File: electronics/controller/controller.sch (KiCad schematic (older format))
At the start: 25 parts

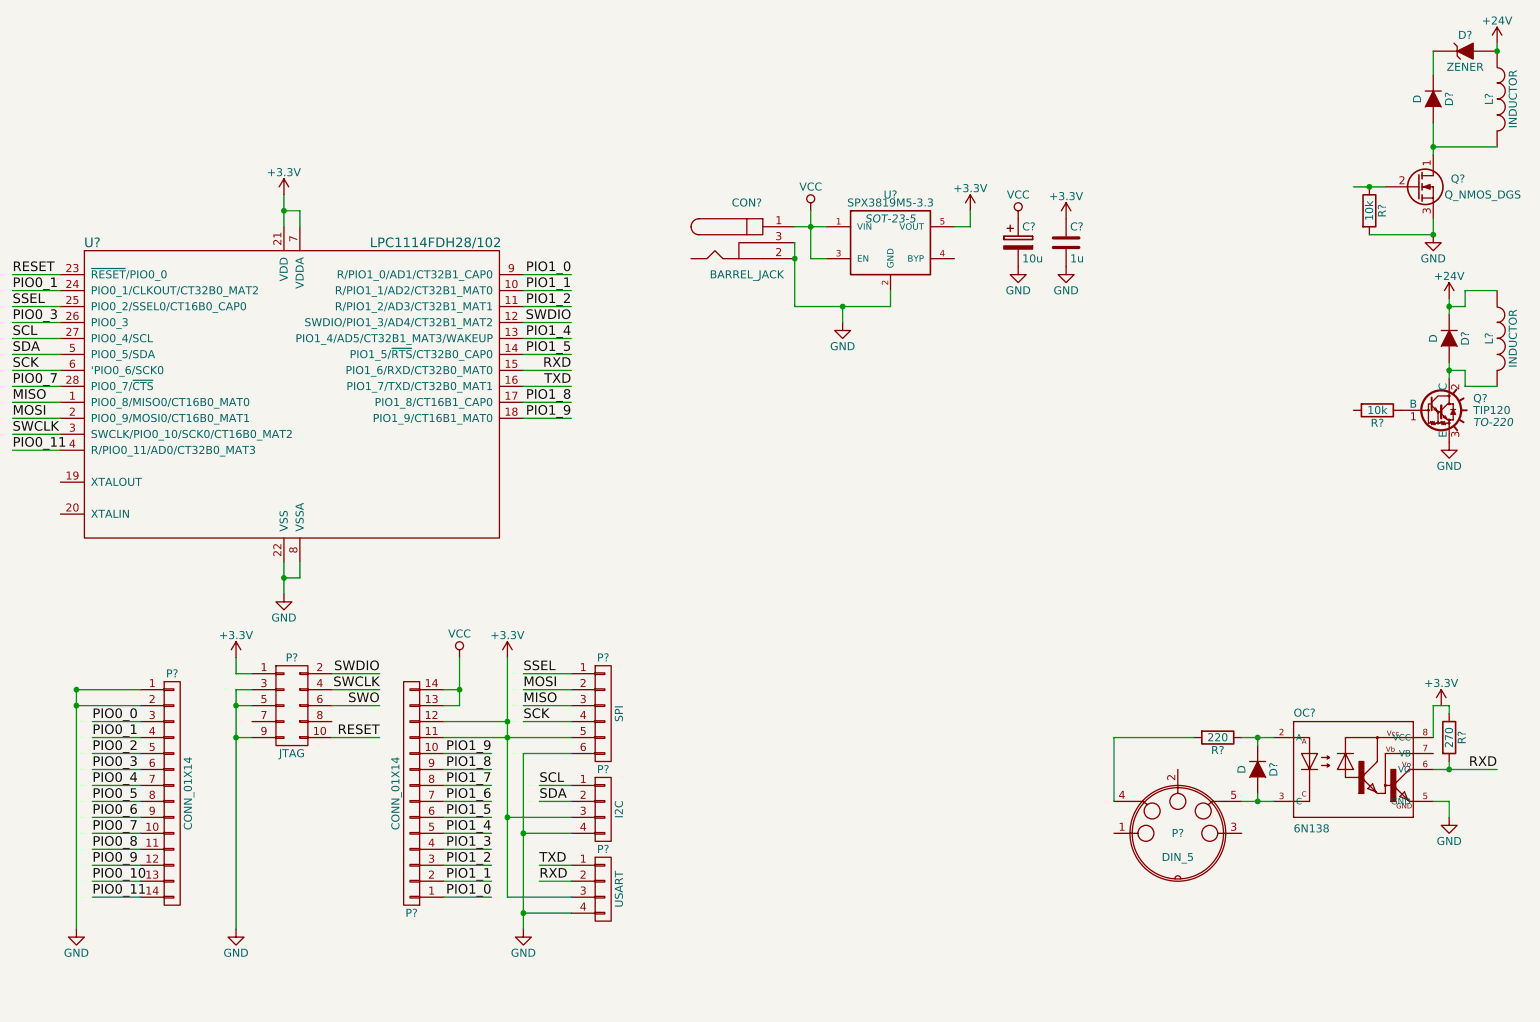
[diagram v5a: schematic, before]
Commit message: Add NFET for reverse polarity protection
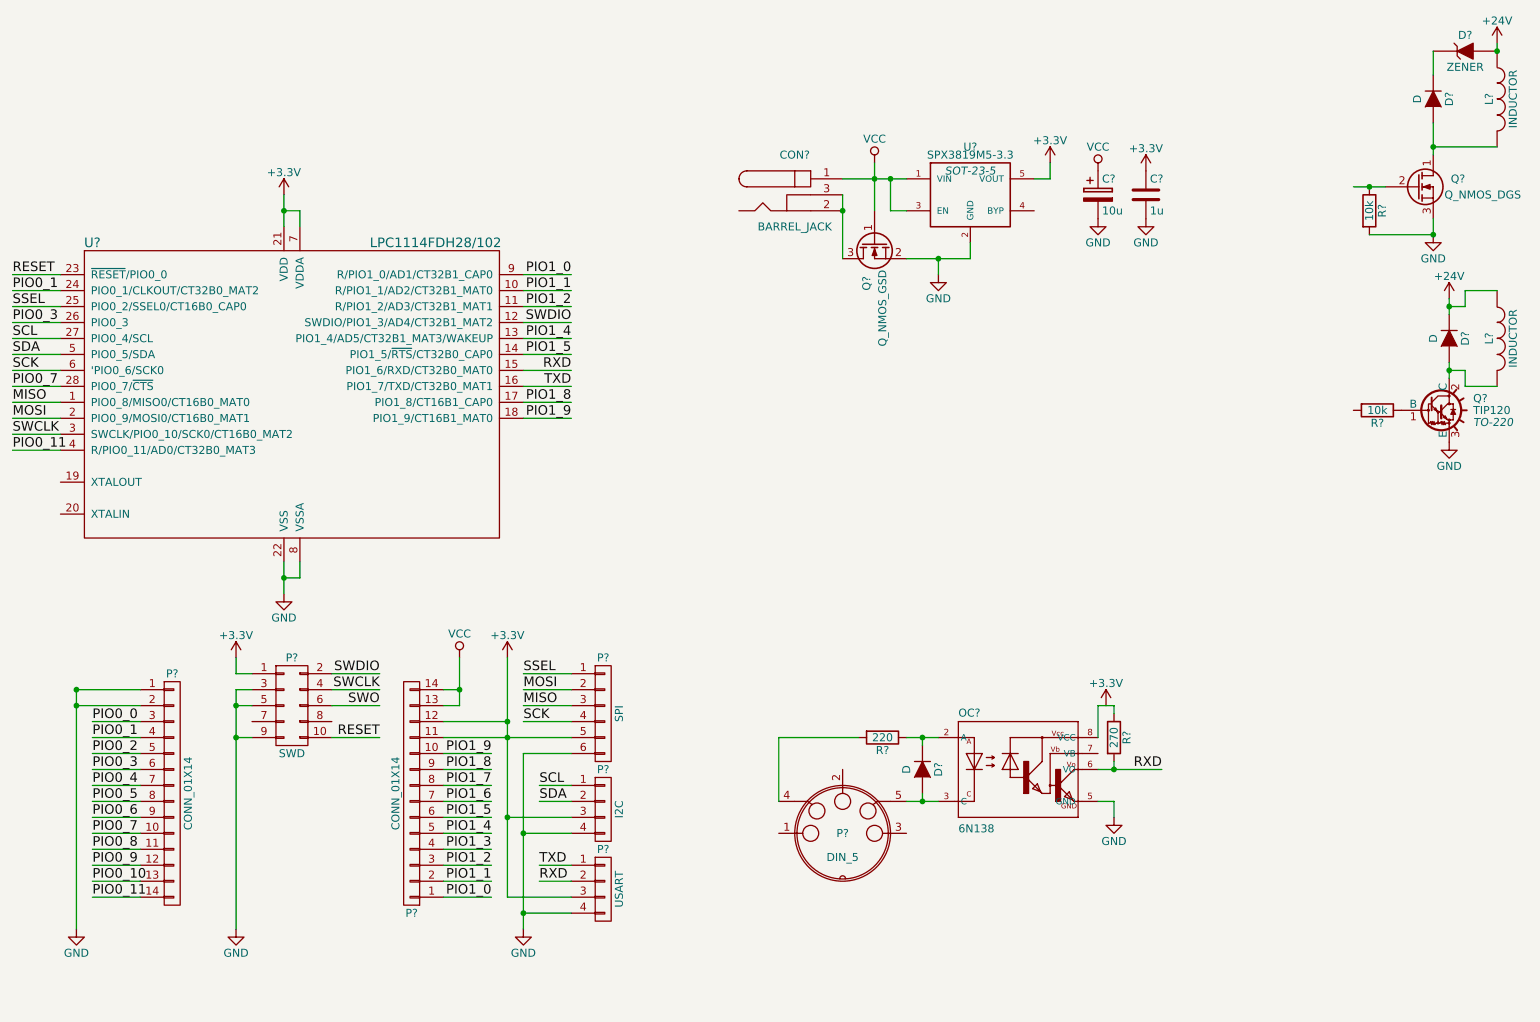
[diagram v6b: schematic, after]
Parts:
- added Q?: Q_NMOS_GSD, symbol Q_NMOS_GSD
- P?: value JTAG -> SWD
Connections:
- net GND: now also Q?.2 (S); no longer CON?.2, CON?.3
- net VCC: now also Q?.1 (G)
- new net: CON?.2, CON?.3, Q?.3 (D)
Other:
- moved on the sheet: C?, CON?, D?, OC?, P?, R?, U?

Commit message: Remove MIDI and solenoid circuits
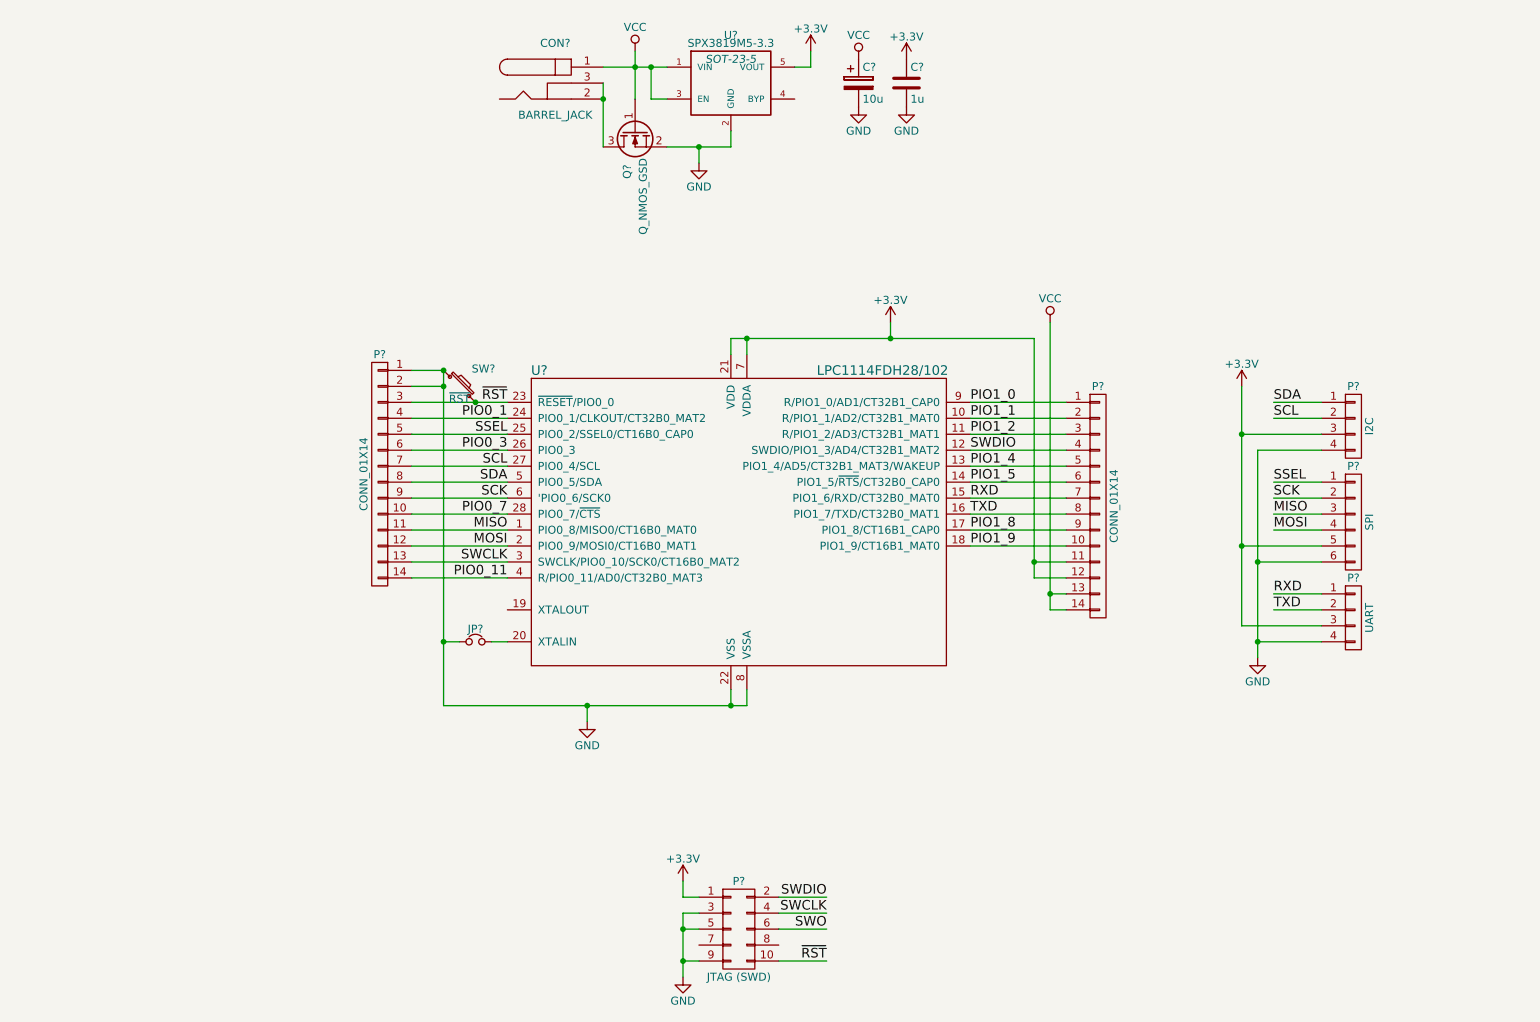
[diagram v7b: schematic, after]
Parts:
- removed D? (x3): D, symbol D
- removed D?: ZENER, symbol ZENER
- removed L? (x2): INDUCTOR, symbol INDUCTOR
- removed OC?: 6N138, optocoupler-DIL08, symbol 6N138
- removed P?: DIN_5, symbol DIN_5
- removed Q?: Q_NMOS_DGS, symbol Q_NMOS_DGS
- removed Q?: TIP120, TO-220, symbol TIP120
- removed R?: 270, symbol R
- removed R?: 220, symbol R
- removed R? (x2): 10k, symbol R
- added JP?: Jumper_NC_Small, symbol Jumper_NC_Small
- added SW?: ~RST~, symbol SW_PUSH_SMALL
- P?: value SWD -> JTAG (SWD)
- P?: value USART -> UART
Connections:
- net PIO0_10 is gone; now on net SWCLK: P?.13 (P13)
- net PIO0_2 is gone; now on net SSEL: P?.5 (P5)
- net PIO0_4 is gone; now on net SCL: P?.7 (P7)
- net PIO0_5 is gone; now on net SDA: P?.8 (P8)
- net PIO0_6 is gone; now on net SCK: P?.9 (P9)
- net PIO0_8 is gone; now on net MISO: P?.11 (P11)
- net PIO0_9 is gone; now on net MOSI: P?.12 (P12)
- net PIO1_3 is gone; now on net SWDIO: P?.4 (P4)
- net PIO1_6 is gone; now on net RXD: P?.7 (P7)
- net PIO1_7 is gone; now on net TXD: P?.8 (P8)
- net RESET is gone; now on net ~RST~: P?.10 (P10), U?.23 (~RESET~/PIO0_0)
- net GND: now also JP?.1, SW?.1
- net MOSI: now also P?.4 (P4); no longer P?.2 (P2)
- net RXD: now also P?.1 (P1); no longer P?.2 (P2)
- net SCK: now also P?.2 (P2); no longer P?.4 (P4)
- net SCL: now also P?.2 (P2); no longer P?.1 (P1)
- net SDA: now also P?.1 (P1); no longer P?.2 (P2)
- net TXD: now also P?.2 (P2); no longer P?.1 (P1)
- net at U?.20 (XTALIN): now also JP?.2
- net PIO0_0 renamed ~RST~
- net ~RST~: now also SW?.2
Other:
- moved on the sheet: C?, CON?, P?, Q?, U?

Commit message: Add LED on PIO0_7 (high-drive output)
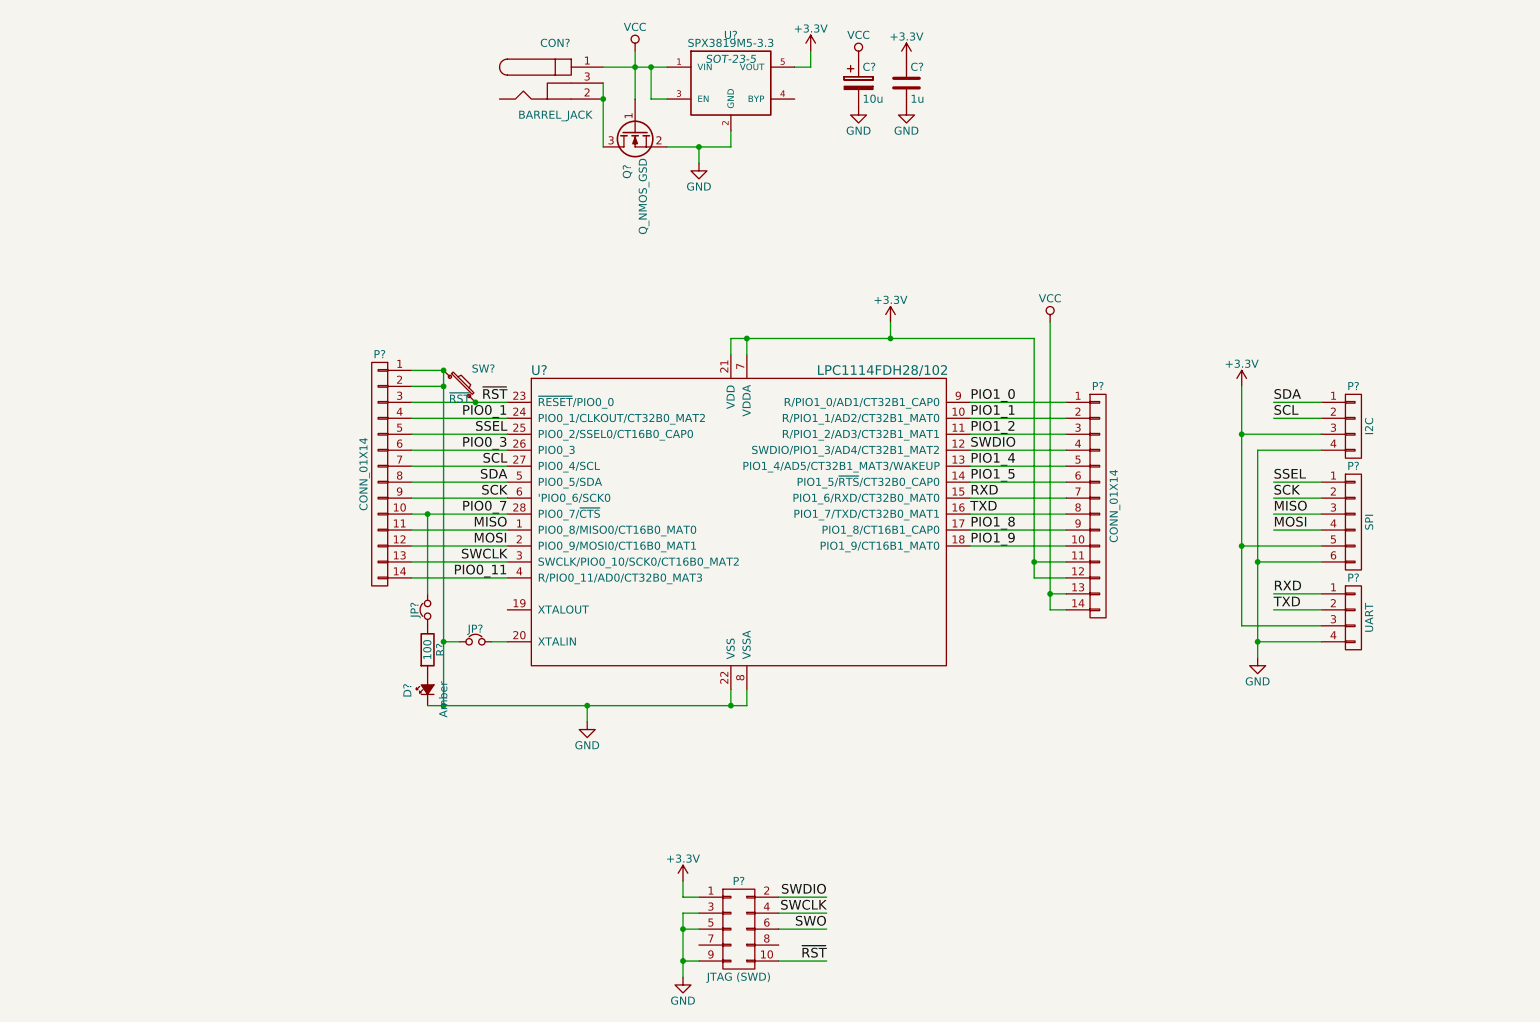
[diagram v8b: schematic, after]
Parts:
- added D?: Amber, symbol Led_Small
- added JP?: Jumper_NC_Small, symbol Jumper_NC_Small
- added R?: 100, symbol R
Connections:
- net GND: now also D?.1 (K)
- net PIO0_7: now also JP?.2
- new net: D?.2 (A), R?.2
- new net: JP?.1, R?.1
